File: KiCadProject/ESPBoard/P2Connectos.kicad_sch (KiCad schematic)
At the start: 7 parts, among them J201 Conn_02x05, J202 Conn_01x02, J203 Conn_02x05, J204 JST_SM04B, J205 DNP, J206 1x05 female, J207 JST_SM04B

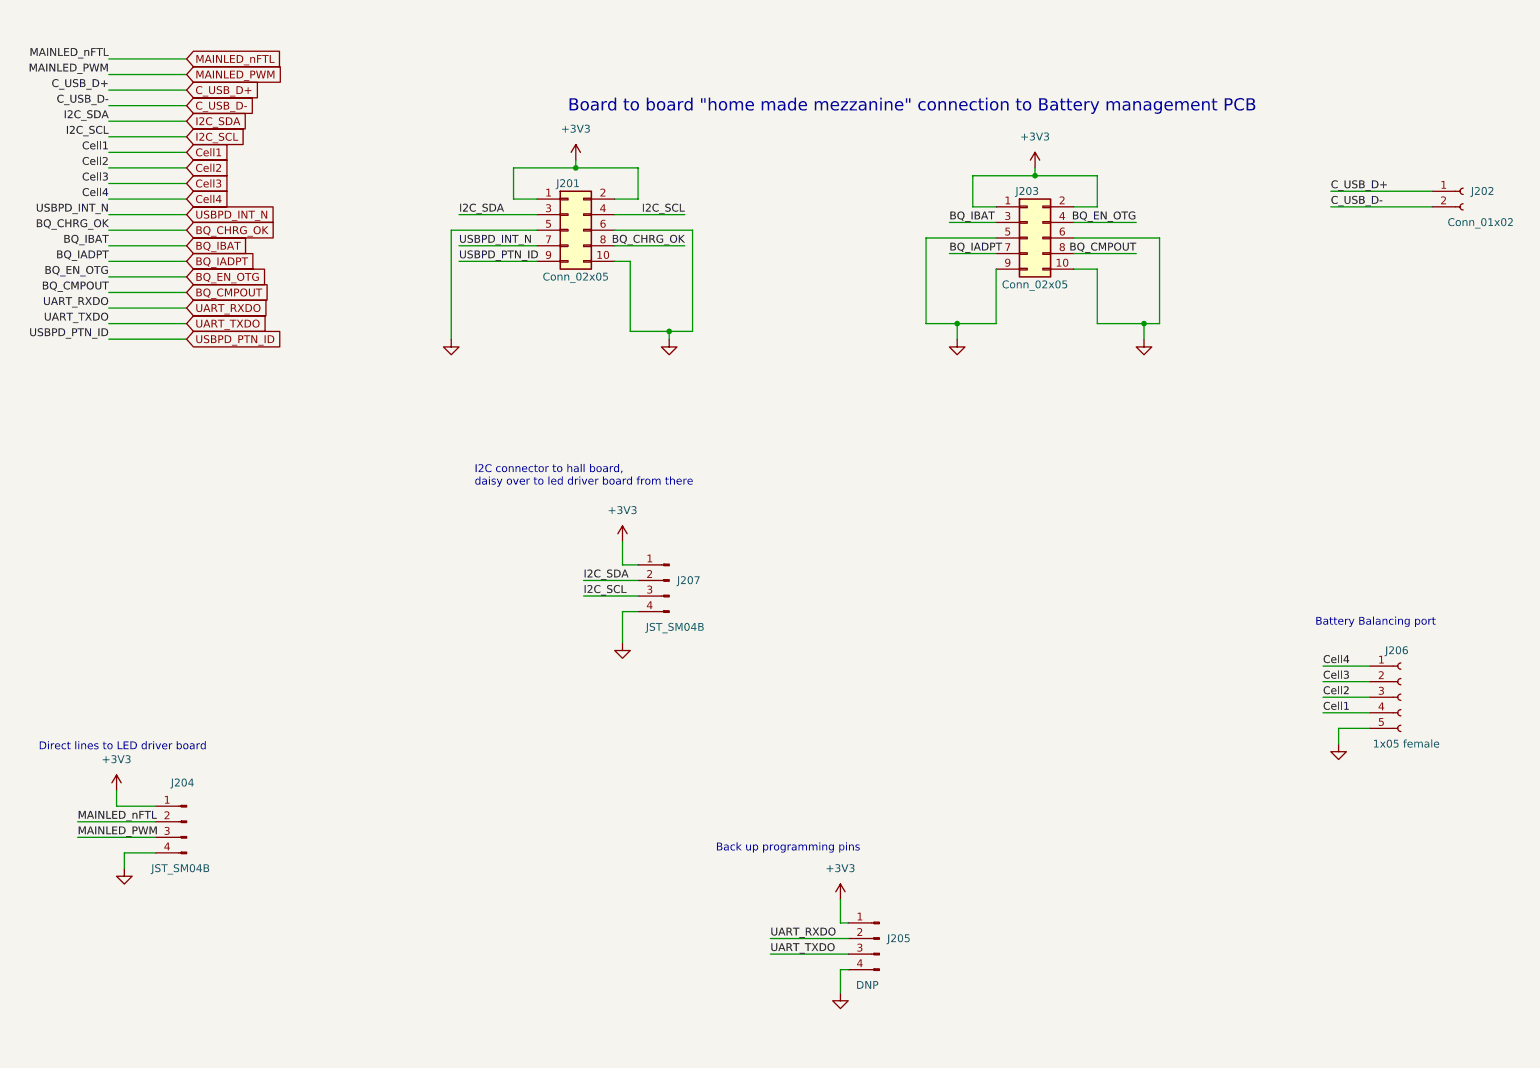
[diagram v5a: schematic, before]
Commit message: Made ready to order PCBs. Some problems with ordering due to misunderstanding. Thinking about solutions
Signed-off-by: Eldalote.Electronics <Eldalote.Electronics@gmail.com>
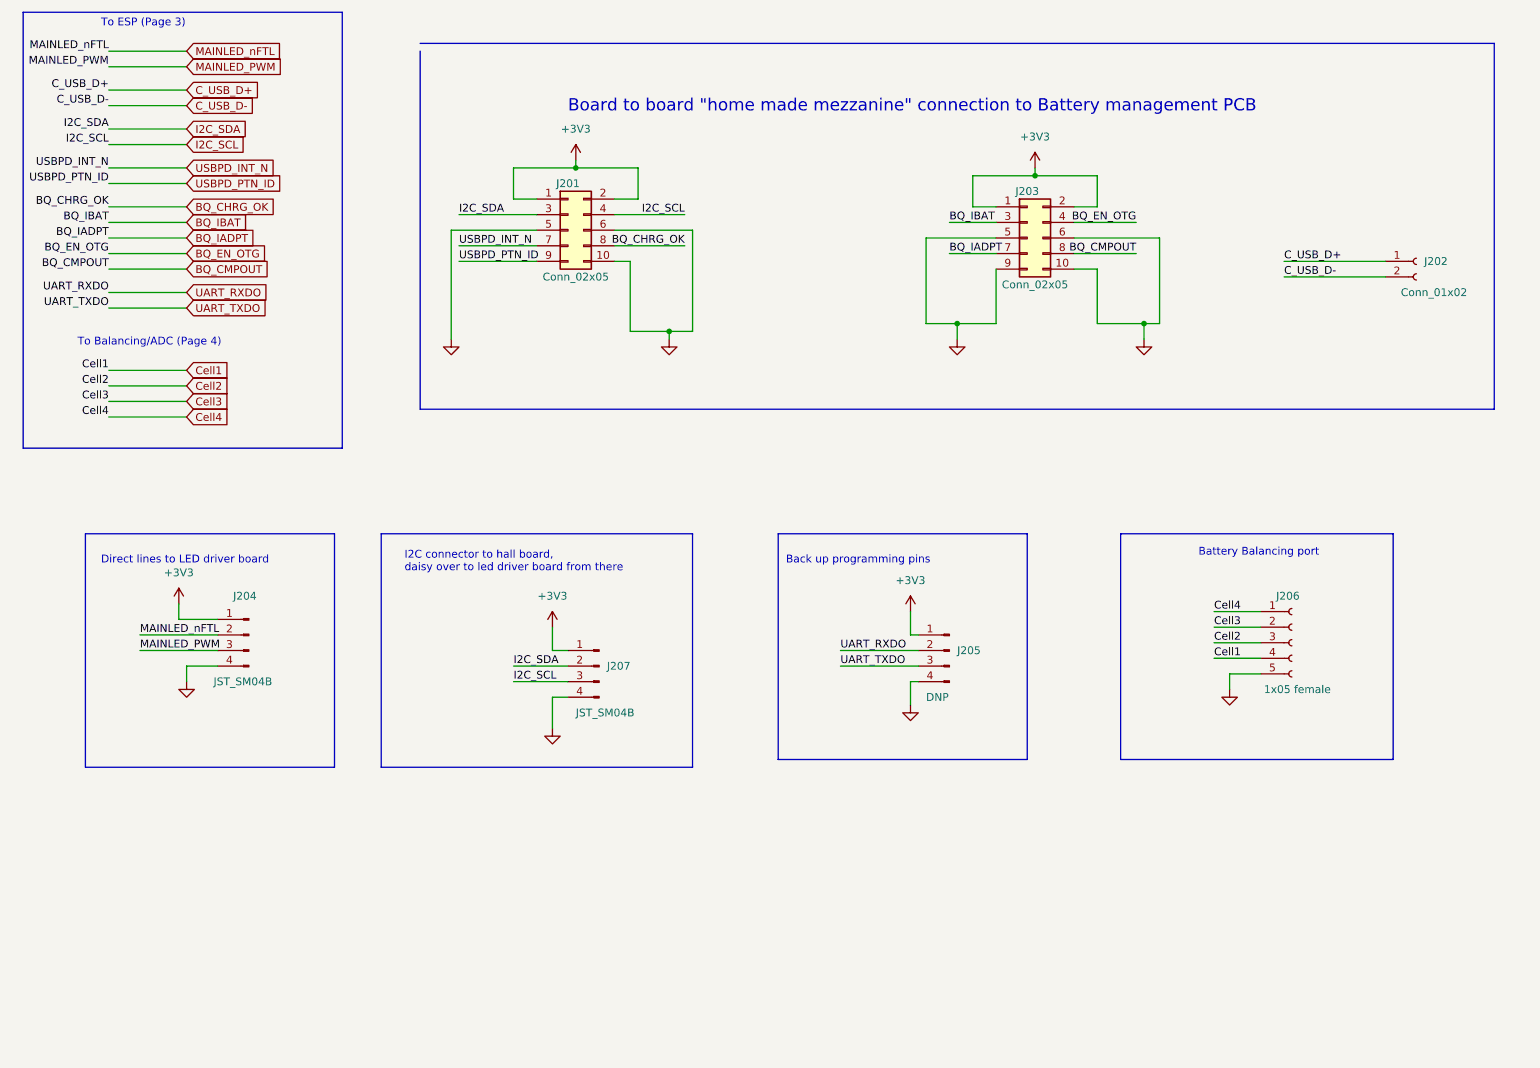
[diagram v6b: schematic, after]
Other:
- note added: "To Balancing/ADC (Page 4)"
- note added: "To ESP (Page 3)"
- company: (none) -> Eldalote Electronics
- title: (none) -> ESP & Feedback Board
- moved on the sheet: J202, J204, J205, J206, J207
